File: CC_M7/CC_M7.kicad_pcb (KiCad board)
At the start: 4 copper layers, 40 x 65 mm, 133 parts, among them J1 Conn_01x04_Pin, J10 Conn_01x04_Pin, J11 USB_B_Micro, J12 Conn_01x04_Pin, J13 Batt_Pins, J3 Conn_01x03_Pin, J4 Conn_01x03_Pin, J5 Conn_01x03_Pin, J6 Conn_01x03_Pin, J7 Conn_01x03_Pin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

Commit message: CCM7A Routing in progress.
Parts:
- JP1, JP10, JP2, JP3, JP4, JP5, JP6, JP7, JP8, JP9: moved to B.Cu
- moved R5 34.9 mm to (103.0, 148.7), turned to 180 degrees
- moved R4 33.8 mm to (103.0, 147.7), turned to 180 degrees
- moved JP9 30.1 mm to (76.7, 131.5)
- moved JP10 24.8 mm to (76.7, 128.8)
- moved JP7 17.6 mm to (76.7, 123.5), turned to 0 degrees
- moved JP2 16.2 mm to (73.2, 123.5), turned to 180 degrees
- moved JP8 14.6 mm to (76.7, 126.2), turned to 0 degrees
- moved JP6 14.5 mm to (76.7, 120.8), turned to 0 degrees
- moved JP3 13.8 mm to (73.2, 126.2), turned to 180 degrees
- moved JP1 12.7 mm to (73.2, 120.8), turned to 180 degrees
- moved JP4 10.0 mm to (73.2, 131.5)
- moved JP5 9.88 mm to (73.2, 128.8)
- moved C30 3.59 mm to (109.7, 162.6)
- moved C58 3.48 mm to (110.8, 118.6), turned to -90 degrees
- moved C31 3.24 mm to (109.0, 115.8)
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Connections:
- U5 pad 10: SPI1_CS3 -> SPI1_SCK
- U5 pad 2: SPI1_CS3_1V8 -> SPI1_SCK_1V8
- U5 pad 3: SPI1_MOSI_1V8 -> SPI1_MISO_1V8
- U5 pad 4: SPI1_MISO_1V8 -> SPI1_MOSI_1V8
- U5 pad 5: SPI1_SCK_1V8 -> SPI1_CS3_1V8
- U5 pad 7: SPI1_SCK -> SPI1_CS3
- U5 pad 8: SPI1_MISO -> SPI1_MOSI
- U5 pad 9: SPI1_MOSI -> SPI1_MISO
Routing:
- net 3V3_RF: track 8.39 -> 65.2 mm, vias 0 -> 8
- net I2C1_SCL: track 0.00 -> 39.1 mm, vias 0 -> 4
- net I2C1_SDA: track 0.00 -> 36.8 mm, vias 0 -> 4
- net SPI1_MISO: track 0.00 -> 32.9 mm, vias 0 -> 5
- net SPI1_SCK: track 0.83 -> 30.3 mm, vias 0 -> 4
- net SPI1_MOSI: track 0.00 -> 27.1 mm, vias 0 -> 4
- net UART1_RX: track 0.00 -> 26.2 mm, vias 0 -> 2
- net UART1_TX: track 0.00 -> 24.9 mm, vias 0 -> 2
- net +5V: track 61.1 -> 83.3 mm, vias 0 -> 4
- net UART2_RX: track 0.00 -> 19.6 mm, vias 0 -> 1
- net NRF_PA_MODE: track 0.00 -> 17.0 mm, vias 0 -> 2
- net UART2_TX: track 0.00 -> 16.5 mm, vias 0 -> 1
- net UART3_RX: track 0.00 -> 15.9 mm, vias 0 -> 2
- net UART3_TX: track 0.27 -> 15.3 mm, vias 0 -> 2
- net SPI1_CS2: track 0.00 -> 14.9 mm, vias 0 -> 4
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
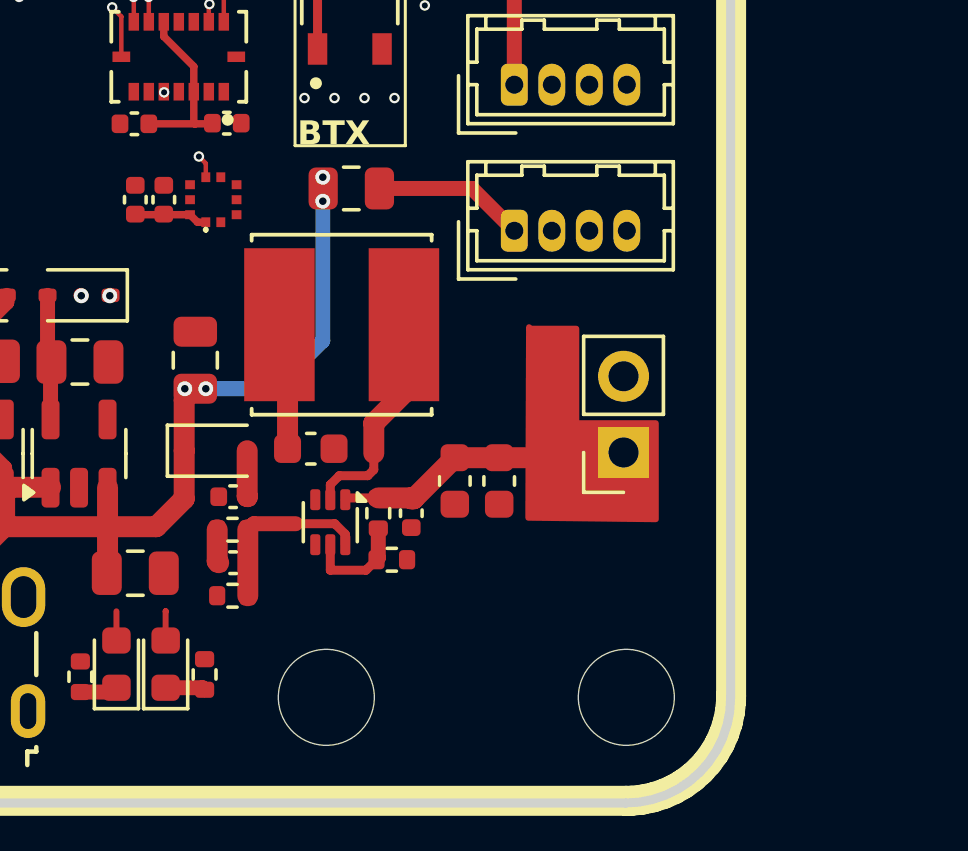
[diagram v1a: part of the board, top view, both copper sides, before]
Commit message: regülatör devresi güvenli kullanıma uygun hale getirildi.
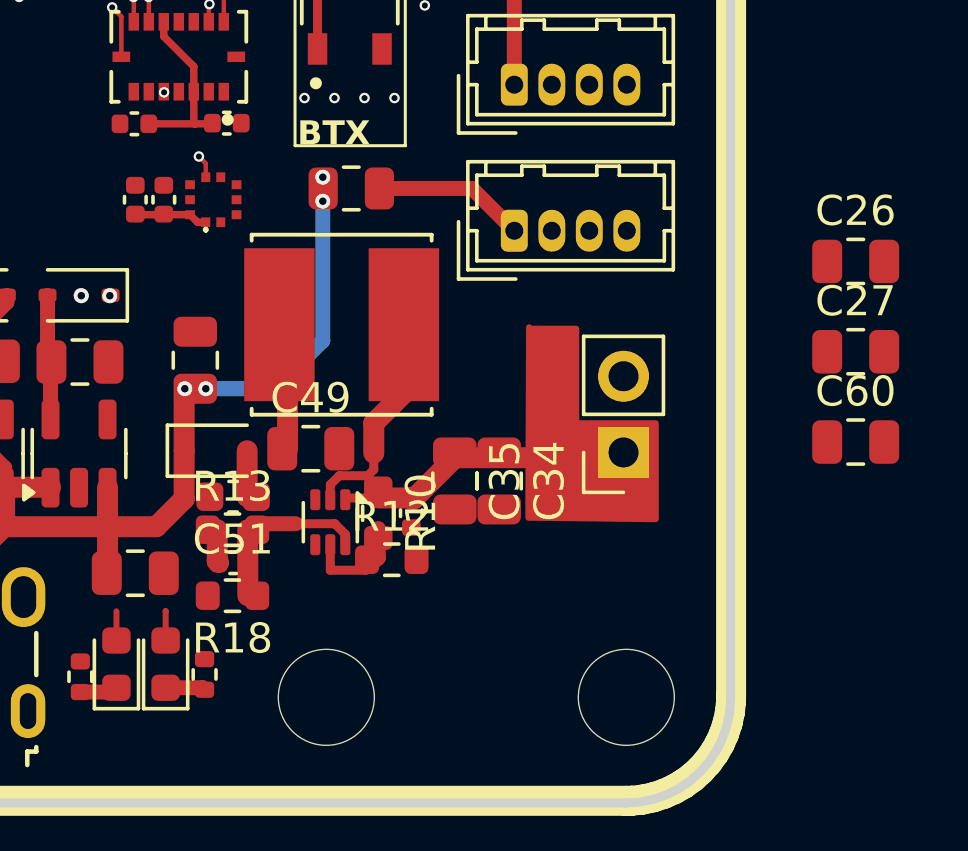
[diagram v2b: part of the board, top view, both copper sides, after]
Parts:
- added C26: 22uF, Capacitor_SMD:C_0805_2012Metric, F.Cu at (131.7, 159.3)
- added C27: 22uF, Capacitor_SMD:C_0805_2012Metric, F.Cu at (131.7, 162.3)
- added C60: 22uF, Capacitor_SMD:C_0805_2012Metric, F.Cu at (131.7, 165.3)
- C34, C35: footprint Capacitor_SMD:C_0603_1608Metric -> Capacitor_SMD:C_0805_2012Metric
- C49: value 22uH -> 22uF; footprint Capacitor_SMD:C_0603_1608Metric -> Capacitor_SMD:C_0805_2012Metric
- C51: footprint Capacitor_SMD:C_0402_1005Metric -> Capacitor_SMD:C_0603_1608Metric
- R10, R12, R13, R18: footprint Resistor_SMD:R_0402_1005Metric -> Resistor_SMD:R_0603_1608Metric

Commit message: CCM7A BIG ROUTING PROGRESS
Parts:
- L6, L7: footprint Inductor_SMD:L_0201_0603Metric -> Inductor_SMD:L_0402_1005Metric
- moved C60 22.8 mm to (109.6, 159.7), turned to 180 degrees
- moved C26 22.5 mm to (109.6, 163.8), turned to 180 degrees
- moved C27 22.1 mm to (109.6, 161.8), turned to 180 degrees
- moved R7 10.0 mm to (101.6, 158.1), turned to 180 degrees
- moved C42 9.73 mm to (108.0, 126.8), turned to -90 degrees
- moved C41 9.39 mm to (102.2, 118.3), turned to 180 degrees
- moved C38 9.34 mm to (102.2, 119.2), turned to 180 degrees
- moved C37 9.32 mm to (109.4, 117.5), turned to 0 degrees
- moved C30 9.16 mm to (102.3, 168.0), turned to 0 degrees
- moved C36 9.09 mm to (109.4, 116.5), turned to 0 degrees
- moved C39 8.82 mm to (107.0, 126.8), turned to 90 degrees
- moved C51 8.32 mm to (114.2, 159.5), turned to 0 degrees
- moved C33 5.52 mm to (102.2, 120.2)
- moved C40 5.12 mm to (101.7, 124.2), turned to 0 degrees
- moved C31 4.22 mm to (110.4, 119.8)
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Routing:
- net UART4_RX: track 0.00 -> 44.9 mm, vias 0 -> 3
- net UART4_TX: track 0.00 -> 42.8 mm, vias 0 -> 3
- net I2C2_SDA: track 0.00 -> 42.0 mm, vias 0 -> 3
- net I2C2_SCL: track 0.00 -> 41.1 mm, vias 0 -> 3
- net NRST: track 4.15 -> 43.6 mm, vias 0 -> 4
- net Net-(D9-A): track 7.26 -> 38.3 mm
- net CAN2_RX: track 0.55 -> 31.4 mm, vias 0 -> 2
- net CAN2_TX: track 0.00 -> 30.5 mm, vias 0 -> 2
- net PA4: track 0.00 -> 24.5 mm, vias 0 -> 2
- net +1V8: track 6.85 -> 27.3 mm, vias 0 -> 4
- net I2C1_SCL: track 39.1 -> 59.4 mm, vias 4 -> 5
- net I2C1_SDA: track 36.8 -> 56.8 mm, vias 4 -> 5
- net PA0: track 7.94 -> 25.6 mm, vias 1 -> 2
- net PC14: track 7.72 -> 24.4 mm, vias 1 -> 2
- net PA1: track 8.17 -> 23.7 mm
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- added copper zone on F.Cu, net +BATT
- added copper zone on In1.Cu, net GND
- removed copper zone on In2.Cu, net GND
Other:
- board text added: "- +"
- board text added: "15V - MAX"
- board text removed: "15V MAX"

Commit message: error check
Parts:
- moved JP1 37.9 mm to (109.2, 132.6), turned to 0 degrees
- moved JP2 37.7 mm to (109.2, 134.5)
- moved JP3 37.5 mm to (109.2, 136.5)
- moved JP5 37.3 mm to (109.2, 138.5)
- moved JP6 37.2 mm to (112.0, 132.7)
- moved JP4 37.2 mm to (109.2, 140.5)
- moved JP7 36.8 mm to (111.7, 134.7)
- moved JP8 36.6 mm to (111.7, 136.7)
- moved JP10 36.4 mm to (111.7, 138.7)
- moved JP9 36.3 mm to (111.7, 140.8)

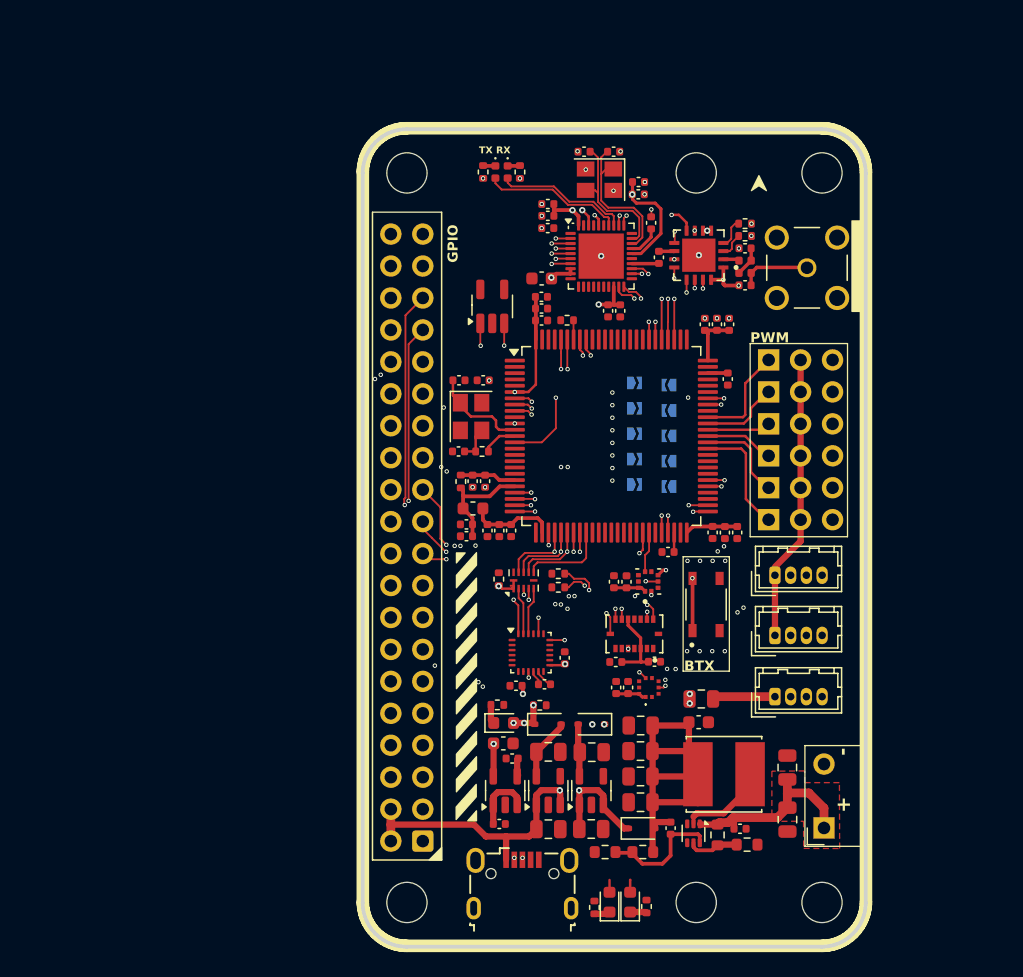
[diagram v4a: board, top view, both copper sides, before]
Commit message: Debugging routes added. / Debug footprint updated.
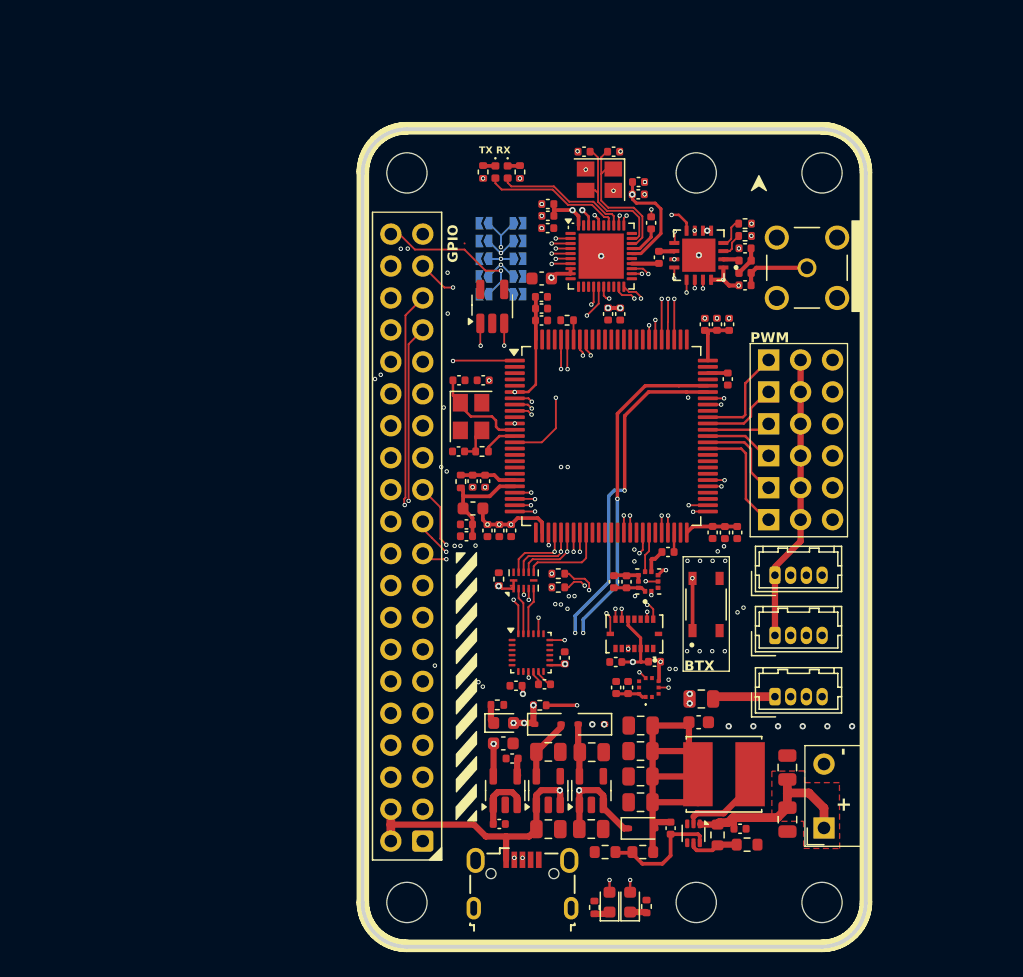
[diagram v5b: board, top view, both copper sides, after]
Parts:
- moved JP4 20.6 mm to (97.0, 124.0), turned to 0 degrees
- moved JP9 20.4 mm to (100.0, 124.0), turned to 180 degrees
- moved JP3 18.5 mm to (97.0, 122.6), turned to 0 degrees
- moved JP8 18.3 mm to (100.0, 122.6), turned to 180 degrees
- moved JP2 18.1 mm to (97.0, 121.2), turned to 0 degrees
- moved JP5 17.9 mm to (97.0, 125.4), turned to 0 degrees
- moved JP7 17.9 mm to (100.0, 121.2), turned to 180 degrees
- moved JP10 17.7 mm to (100.0, 125.4), turned to 180 degrees
- moved JP1 17.7 mm to (97.0, 119.8)
- moved JP6 17.6 mm to (100.0, 119.8), turned to 180 degrees
- moved C39 0.25 mm to (107.0, 127.0)
- moved C42 0.25 mm to (108.0, 127.0)
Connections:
- JP1 pad 1: +3.3V -> J2_31
- JP1 pad 2: J2_31 -> +3.3V
- JP2 pad 1: SWDIO -> J2_32
- JP2 pad 2: J2_32 -> SWDIO
- JP3 pad 1: SWCLK -> J2_34
- JP3 pad 2: J2_34 -> SWCLK
- JP4 pad 1: SWO -> J2_36
- JP4 pad 2: J2_36 -> SWO
- JP5 pad 1: NRST -> J2_40
- JP5 pad 2: J2_40 -> NRST
- JP9 pad 1: unconnected-(JP9-A-Pad1) -> J2_36
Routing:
- net USB_DP: track 0.00 -> 49.0 mm, vias 1 -> 4
- net USB_DM: track 0.00 -> 46.7 mm, vias 1 -> 3
- net LED0: track 0.97 -> 31.9 mm, vias 0 -> 2
- net LED1: track 0.98 -> 31.9 mm, vias 0 -> 2
- net J2_31: track 0.00 -> 21.5 mm, vias 0 -> 2
- net J2_32: track 0.00 -> 20.5 mm, vias 0 -> 2
- net J2_34: track 0.00 -> 15.2 mm, vias 0 -> 3
- net PE2: track 0.00 -> 13.9 mm, vias 0 -> 2
- net J2_40: track 0.00 -> 13.7 mm, vias 0 -> 1
- net J2_36: track 0.00 -> 12.7 mm, vias 0 -> 1
- net 3V3_RF: track 55.5 -> 66.5 mm, vias 6 -> 7
- net SPI3_CS: track 1.40 -> 9.27 mm, vias 1 -> 2
- net SPI3_IRQ: track 1.41 -> 9.07 mm, vias 1 -> 2
- net GND: track 10.2 -> 16.2 mm, vias 42 -> 43
- net NRF_NRST: track 0.00 -> 1.23 mm, vias 0 -> 1
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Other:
- board text added: "NRF52 ."
- board text added: "STM32 ."
- board text removed: "NRF52"
- board text removed: "STM32"

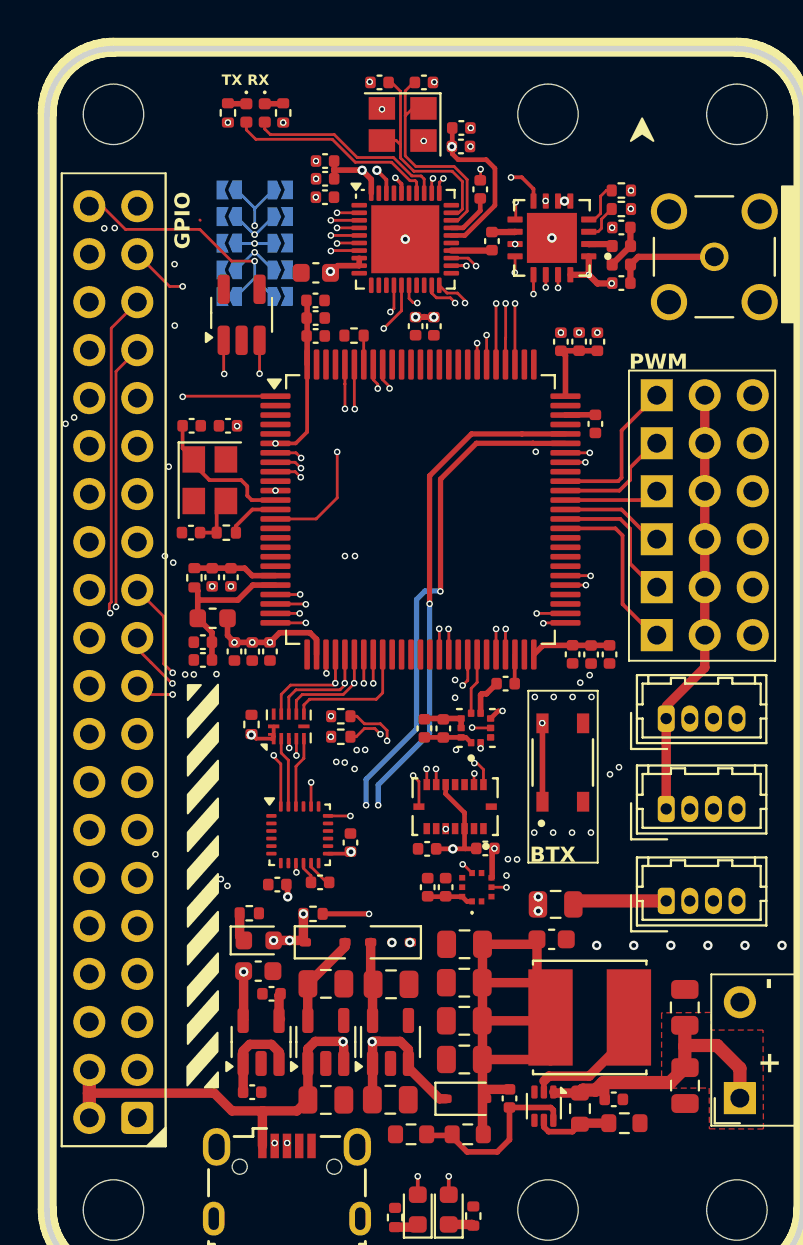
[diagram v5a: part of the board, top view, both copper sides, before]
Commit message: Routing Completed 0 Error
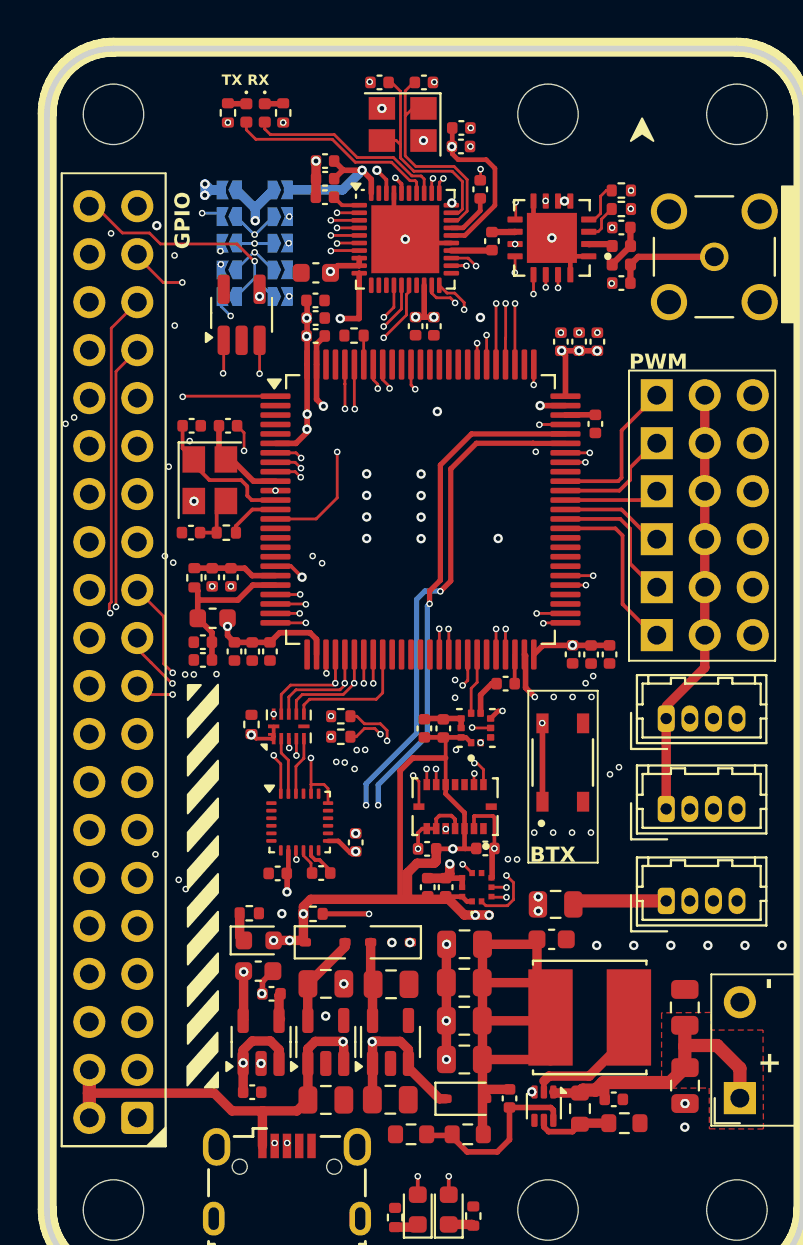
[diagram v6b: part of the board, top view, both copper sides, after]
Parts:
- moved U13 0.68 mm to (100.9, 153.2)
- moved C52 0.59 mm to (99.7, 156.0)
- moved C57 0.50 mm to (102.0, 155.9)
- moved C56 0.28 mm to (103.8, 154.3)
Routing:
- net GND: track 16.2 -> 61.9 mm, vias 43 -> 61
- net +3.3V: track 44.3 -> 84.3 mm, vias 12 -> 32
- net SWDIO: track 0.00 -> 33.8 mm, vias 0 -> 3
- net SWCLK: track 0.00 -> 22.8 mm, vias 0 -> 2
- net SWO: track 0.00 -> 16.3 mm, vias 0 -> 2
- net NRST: track 43.6 -> 55.9 mm, vias 4 -> 5
- net 3V3_RF: track 66.5 -> 77.9 mm, vias 7 -> 8
- net NRF_SWCLK: track 1.82 -> 12.8 mm, vias 1 -> 2
- net NRF_SWDIO: track 1.86 -> 12.6 mm, vias 1 -> 2
- net NRF_NRST: track 1.23 -> 9.24 mm, vias 1 -> 2
- net I2C1_SCL: track 59.3 -> 62.4 mm
- net +1V8: track 27.3 -> 29.2 mm
- net J2_31: track 21.5 -> 19.9 mm
- net DEC1: track 0.00 -> 1.51 mm
- net I2C2_SDA: track 42.0 -> 43.2 mm
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
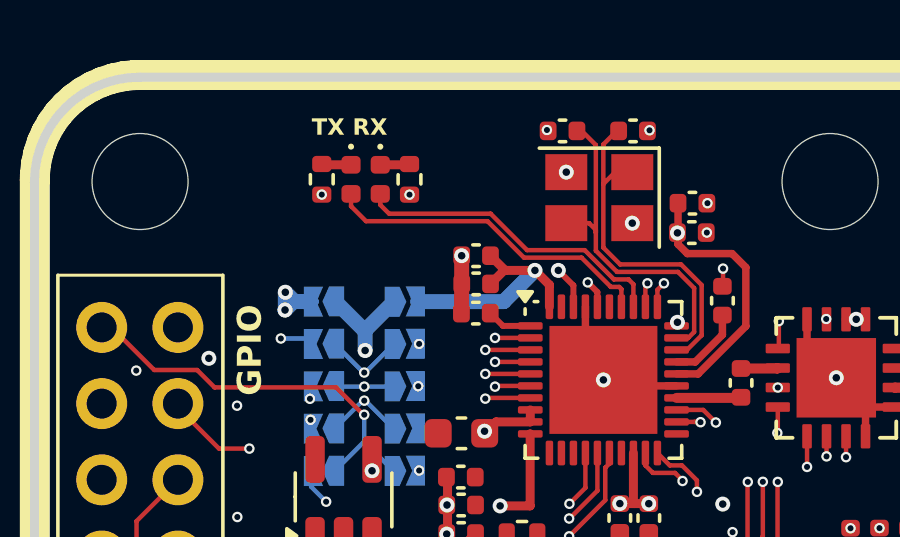
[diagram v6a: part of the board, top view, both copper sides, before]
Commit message: BOM finished.
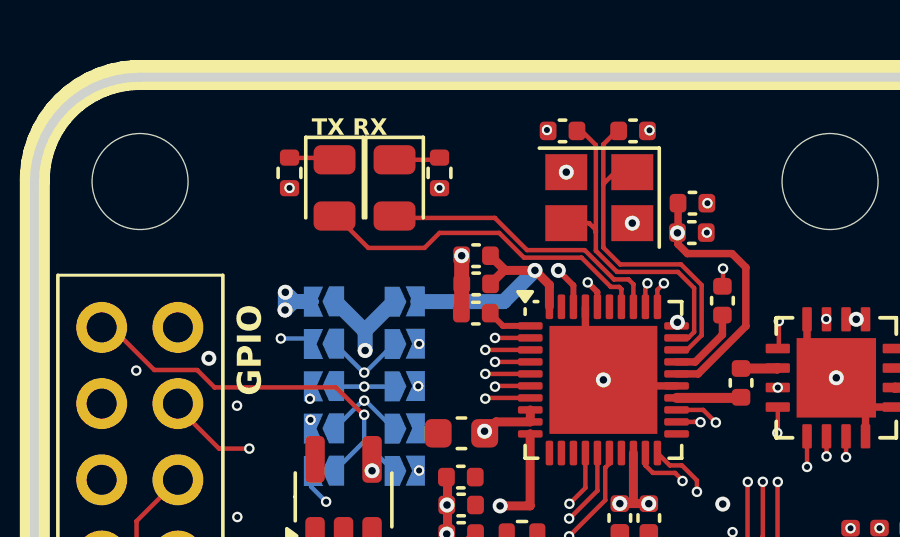
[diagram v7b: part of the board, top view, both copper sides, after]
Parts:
- C20, C21: value 12pF -> 8pF
- C32, C44: value 16pF -> 8pF
- D5, D6: footprint LED_SMD:LED_0402_1005Metric -> LED_SMD:LED_0805_2012Metric
- L1: value SRN6045TA-2R2Y -> 2.2uH
- U8: value TPS562206 -> TPS566242DRL
- moved R2 1.10 mm to (96.0, 115.5)
- moved R17 1.02 mm to (101.0, 115.5)
- moved D5 0.62 mm to (97.5, 116.0)
- moved D6 0.55 mm to (99.5, 116.0)
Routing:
- net NRF_LED1: track 10.6 -> 9.65 mm
- net Net-(D6-K): track 0.99 -> 1.53 mm
- net Net-(D5-K): track 0.99 -> 1.50 mm

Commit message: Rotation check completed.
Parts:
- moved U9 0.71 mm to (105.7, 165.6), turned to 0 degrees
- moved U10 0.06 mm to (102.2, 164.9), turned to 0 degrees
- turned U12 to -90 degrees
- turned U1 to -90 degrees
- turned U13 to -90 degrees
- turned U2 to 0 degrees
- turned U3 to 90 degrees
- turned U5 to 0 degrees
- turned U8 to 180 degrees
